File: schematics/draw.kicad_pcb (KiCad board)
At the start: 2 copper layers, 36.2 x 35.6 mm, 33 parts, among them P1 I2C, P2 UART, P3 DBG, P4 USB_OTG, P5 Power_IN, P6 Power_OUT, SW1 SW_Push, U1 EFM32HG309, U2 TPD4E002, U3 INA260

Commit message: first layout
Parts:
- added REF**: MountingHole_2.2mm_M2, Mounting_Holes:MountingHole_2.2mm_M2, F.Cu at (62.7, 132.3)
- added REF**: MountingHole_2.2mm_M2, Mounting_Holes:MountingHole_2.2mm_M2, F.Cu at (62.7, 97.7)
- added REF**: MountingHole_2.2mm_M2, Mounting_Holes:MountingHole_2.2mm_M2, F.Cu at (107.3, 132.3)
- added REF**: MountingHole_2.2mm_M2, Mounting_Holes:MountingHole_2.2mm_M2, F.Cu at (107.2, 97.8)
- P1: value I2C -> I2C Conn
- P2: value UART -> UART Conn
- P3: value DBG -> Debug Conn
- R11, R9: value NP -> 0R_NP
- moved P3 58.9 mm to (94.4, 107.5)
- moved SW1 40.2 mm to (87.3, 132.2)
- moved P4 30.3 mm to (107.2, 113.1)
- moved D1 29.8 mm to (107.7, 120.4)
- moved R8 29.8 mm to (107.7, 125.5)
- moved C2 29.2 mm to (90.0, 120.8), turned to 180 degrees
- moved L1 28.7 mm to (102.1, 115.7)
- moved U1 24.0 mm to (88.5, 114.9)
- moved R7 22.7 mm to (95.3, 111.2)
- moved R6 22.6 mm to (95.4, 113.4)
- moved C6 22.0 mm to (96.4, 118.2), turned to 270 degrees
- moved U2 20.7 mm to (103.3, 109.7)
- moved P1 20.5 mm to (95.0, 125.2)
- moved P2 19.7 mm to (101.6, 125.2)
- moved C3 19.6 mm to (93.6, 118.2), turned to 270 degrees
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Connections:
- P1 pad 2: /MCU/I2C0-SDA -> /MCU/I2C0_SCL
- P1 pad 3: /MCU/I2C0_SCL -> /MCU/I2C0-SDA
- U1 pad 21: Net-(U1-Pad21) -> GND
- U2 pad 4: Net-(P4-Pad3) -> Net-(P4-Pad2)
- U2 pad 5: Net-(P4-Pad2) -> Net-(P4-Pad3)
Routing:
- net /MCU/I2C0_SCL: track 0.00 -> 35.7 mm, vias 0 -> 3
- net GND: track 0.00 -> 33.5 mm, vias 0 -> 8
- net /MCU/I2C0-SDA: track 0.00 -> 30.6 mm, vias 0 -> 1
- net Net-(P2-Pad3): track 0.00 -> 28.5 mm, vias 0 -> 1
- net +3.3VA: track 11.0 -> 39.3 mm, vias 0 -> 3
- net /MCU/UART_TX: track 0.00 -> 27.9 mm, vias 0 -> 1
- net Net-(SW1-Pad1): track 0.00 -> 21.4 mm, vias 0 -> 2
- net Net-(P4-Pad2): track 0.00 -> 14.0 mm, vias 0 -> 2
- net +3V3: track 0.00 -> 13.2 mm, vias 0 -> 2
- net /Current Sense Amplifier/ALERT: track 5.94 -> 18.5 mm
- net Net-(P4-Pad3): track 0.00 -> 12.5 mm
- net Net-(C1-Pad1): track 0.00 -> 12.2 mm
- net /Current Sense Amplifier/I2C_SDA: track 4.35 -> 12.5 mm
- net /MCU/GPIO_PB11: track 0.00 -> 6.89 mm
- net /MCU/SWD_CLK: track 0.00 -> 6.50 mm
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- added copper zone on F.Cu, net +3V3
- added copper zone on B.Cu, net GND
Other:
- board size 36.2 x 35.6 mm -> 50 x 40 mm
- rule via_min_drill: 0.3302 -> 0.3
- rule via_min_size: 0.6858 -> 0.6

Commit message: second layout
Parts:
- moved C3 3.59 mm to (96.3, 115.7), turned to 0 degrees
- moved L1 1.61 mm to (102.1, 117.3)
- moved C1 1.54 mm to (98.7, 119.7)
- moved C6 1.50 mm to (96.4, 119.7)
- moved C2 1.47 mm to (91.4, 120.8)
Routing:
- net +3V3: track 13.2 -> 18.5 mm
- net Net-(L1-Pad1): track 3.10 -> 4.66 mm
- net GND: track 33.5 -> 32.5 mm
- net Net-(C1-Pad1): track 12.2 -> 12.9 mm

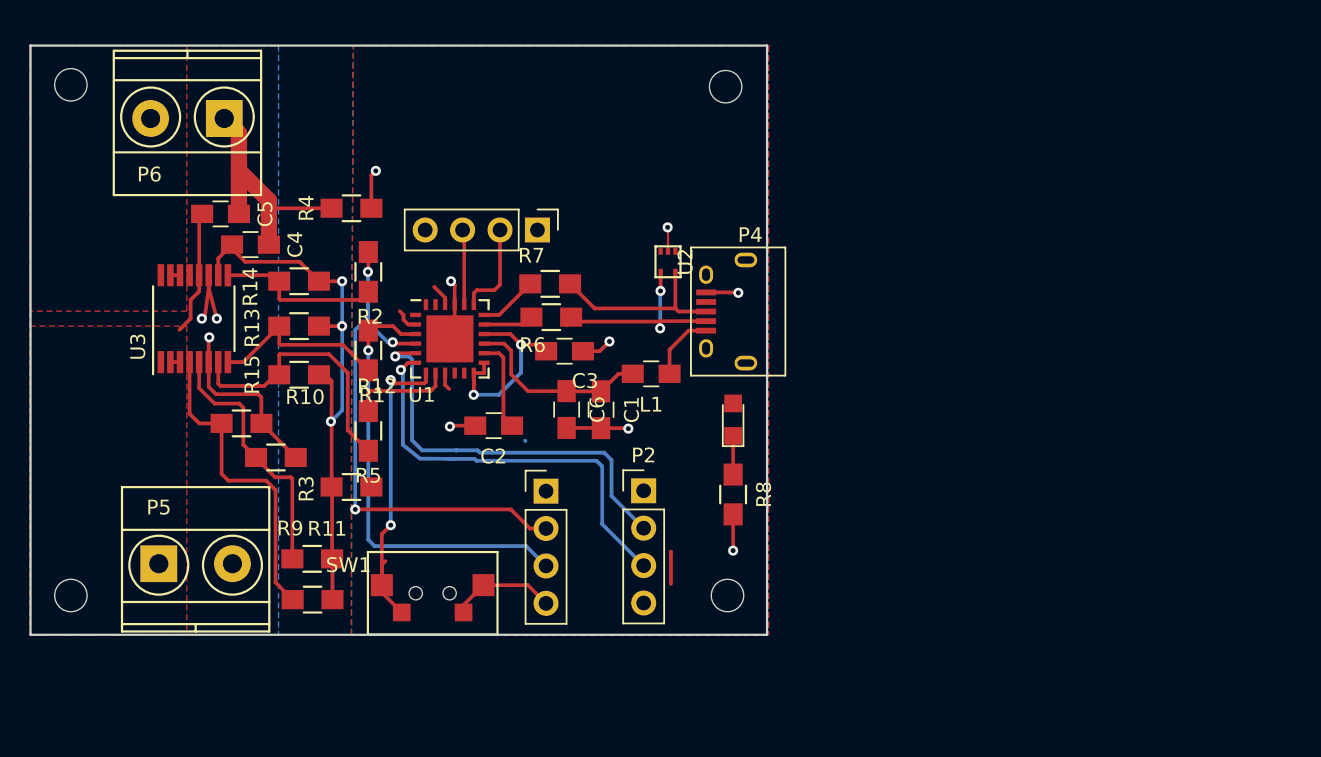
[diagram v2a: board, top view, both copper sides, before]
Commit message: third layout, passes drc
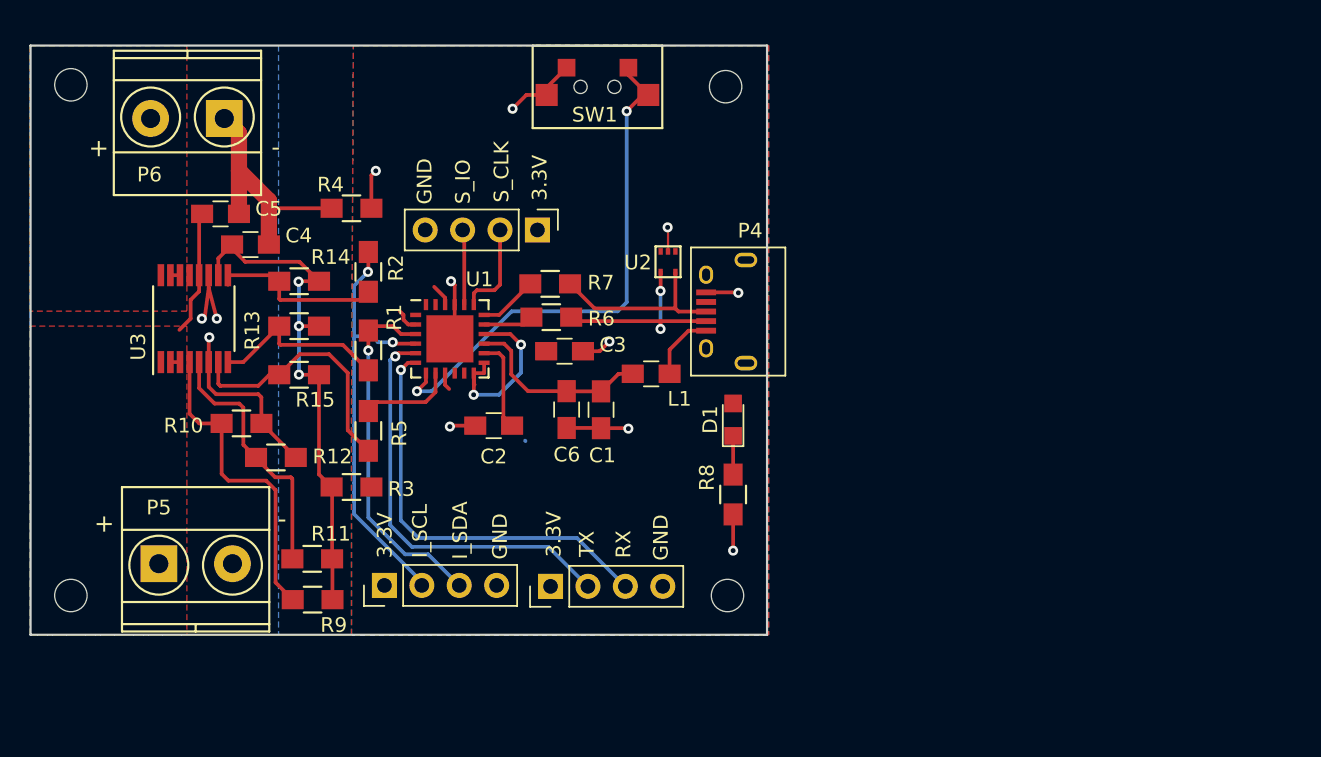
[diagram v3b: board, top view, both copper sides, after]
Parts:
- P1: value I2C Conn -> I2C
- P2: value UART Conn -> UART
- P3: value Debug Conn -> DBG
- R11, R9: value 0R_NP -> NP
- moved SW1 36.2 mm to (98.5, 97.8), turned to 180 degrees
- moved P1 12.7 mm to (84.0, 131.6), turned to 90 degrees
- moved P2 9.06 mm to (95.3, 131.7), turned to 90 degrees
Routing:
- net Net-(SW1-Pad1): track 21.4 -> 35.6 mm
- net /MCU/I2C0_SCL: track 35.7 -> 29.3 mm, vias 3 -> 2
- net /MCU/I2C0-SDA: track 30.6 -> 24.3 mm
- net +3.3VA: track 39.3 -> 36.5 mm
- net (no net): track 2.24 -> 0.04 mm
- net GND: track 32.5 -> 30.5 mm, vias 8 -> 9
- net +3V3: track 18.5 -> 17.2 mm
- net /Current Sense Amplifier/ALERT: track 18.5 -> 17.6 mm
- net /MCU/GPIO_PB11: track 6.89 -> 6.38 mm
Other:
- net class Default: clearance 0.254 -> 0.1524
- rule trace_clearance: 0.254 -> 0.1524
- board text added: "+"
- board text added: "-"
- board text added: "3.3V"
- board text added: "GND"
- board text added: "I_SCL"
- board text added: "I_SDA"
- board text added: "RX"
- board text added: "S_CLK"
- board text added: "S_IO"
- board text added: "TX"
